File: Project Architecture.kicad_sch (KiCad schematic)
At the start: 0 parts

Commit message: Finished 65% of schematics
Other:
- sheet Section A - Title A renamed MCU - Unit
- sheet Section B - Title B renamed Power - Battery Management
- added sheet Logic - I2C Mux (Logic_I2C_Mux.kicad_sch)
- added sheet Misc - Mounting Holes & Fiducials (Misc - Mounting Holes.kicad_sch)
- added sheet Motor Control - Drivers (Motor_Control_Drivers.kicad_sch)
- added sheet Power - Path & Generation (Power_Path_Generation.kicad_sch)
- added sheet Power - Wireless Receiver & USB (Power_Wireless_Receiver_USB.kicad_sch)
- sheet MCU - Unit: file Section A - Title A.kicad_sch -> MCU_Unit.kicad_sch
- sheet Power - Battery Management: file Section B - TItle B.kicad_sch -> Power_Battery_Management.kicad_sch
- sheet Power - Battery Management ports: added +VBAT, +VCHARGE; removed none
- note added: "Page 6"
- note added: "Page 7"
- note added: "Page 9"

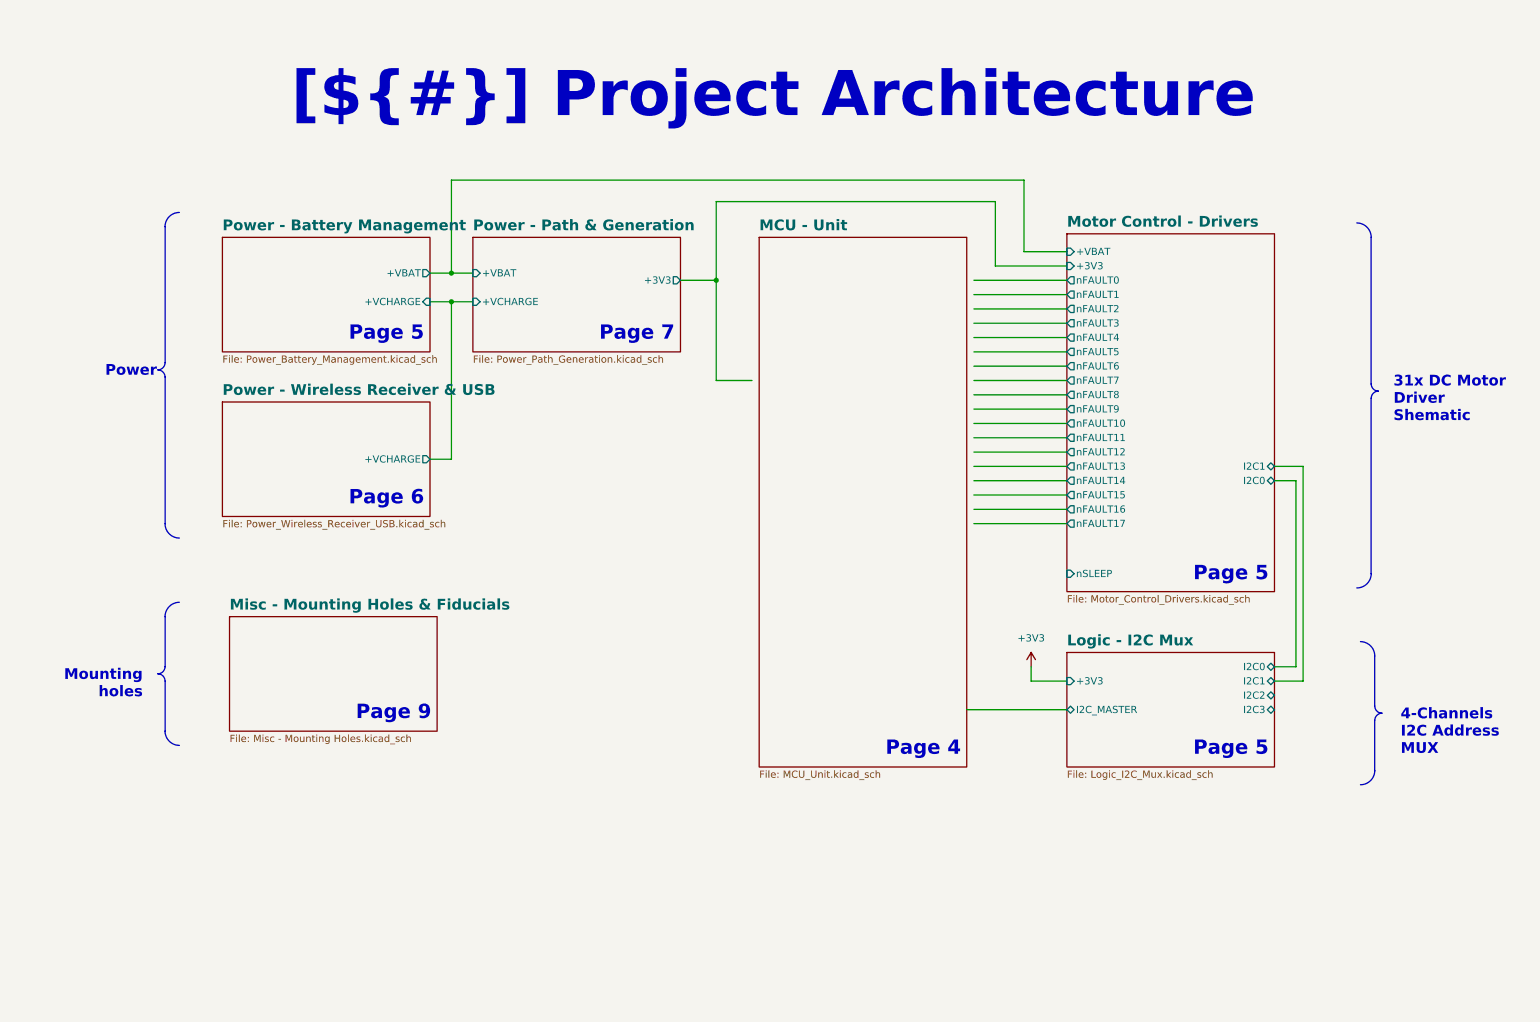
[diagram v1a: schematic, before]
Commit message: Added footprints, images, almost finished all èages except for the MCU
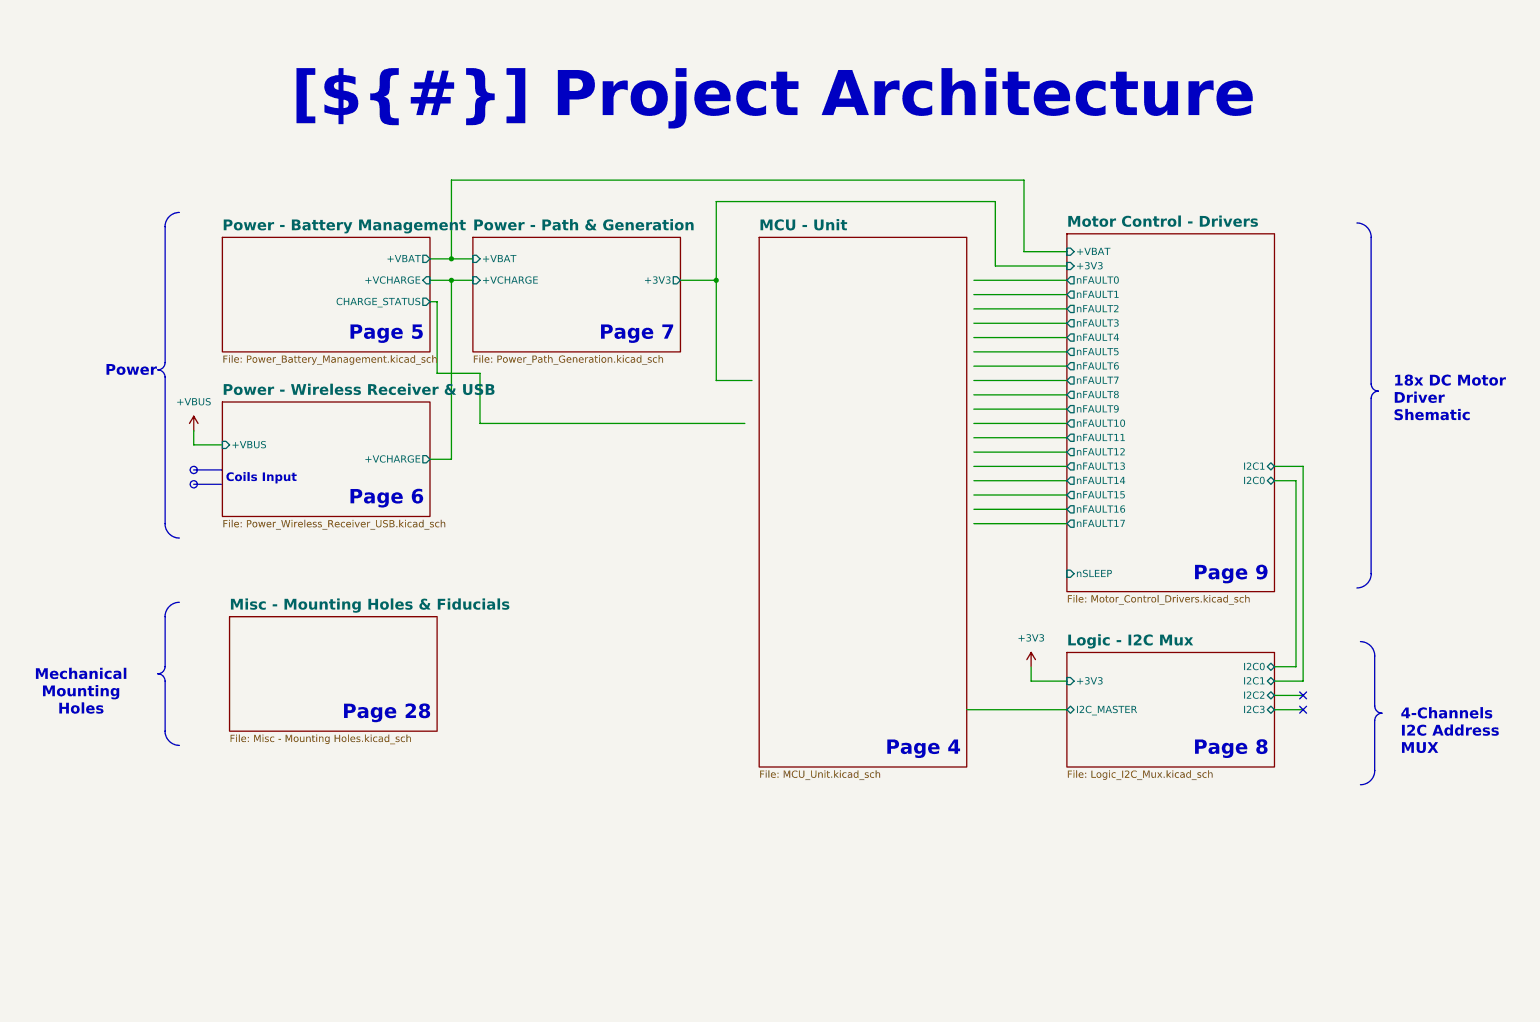
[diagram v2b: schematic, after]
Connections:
- no-connect marks 0 -> 2
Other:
- sheet Power - Battery Management ports: added CHARGE_STATUS; removed none
- sheet Power - Wireless Receiver & USB ports: added +VBUS; removed none
- note added: "Page 28"
- note added: "Page 8"

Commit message: Added RGB LED, added motor connectors, added test points, imported all 3D models
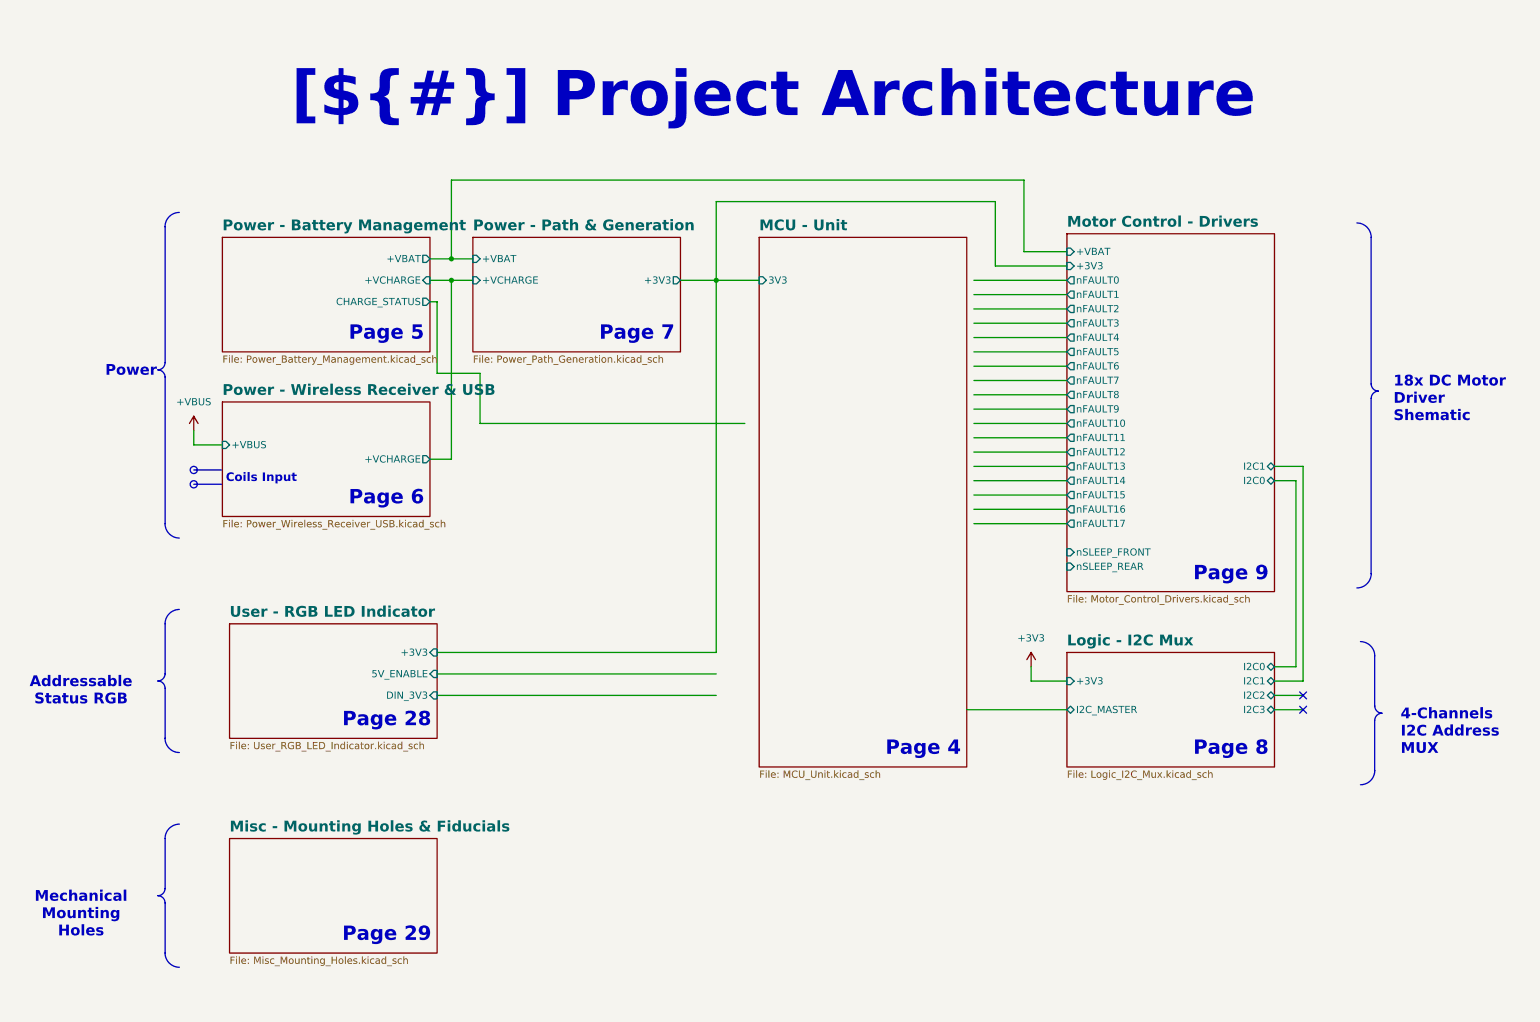
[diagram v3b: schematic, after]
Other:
- added sheet User - RGB LED Indicator (User_RGB_LED_Indicator.kicad_sch)
- sheet MCU - Unit ports: added 3V3; removed none
- sheet Misc - Mounting Holes & Fiducials: file Misc - Mounting Holes.kicad_sch -> Misc_Mounting_Holes.kicad_sch
- sheet Motor Control - Drivers ports: added nSLEEP_FRONT, nSLEEP_REAR; removed nSLEEP
- note added: "Page 29"

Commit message: Finished schematic, imported all footprints, all 3D models and created STM32 project, now need to proofread shematic before layout
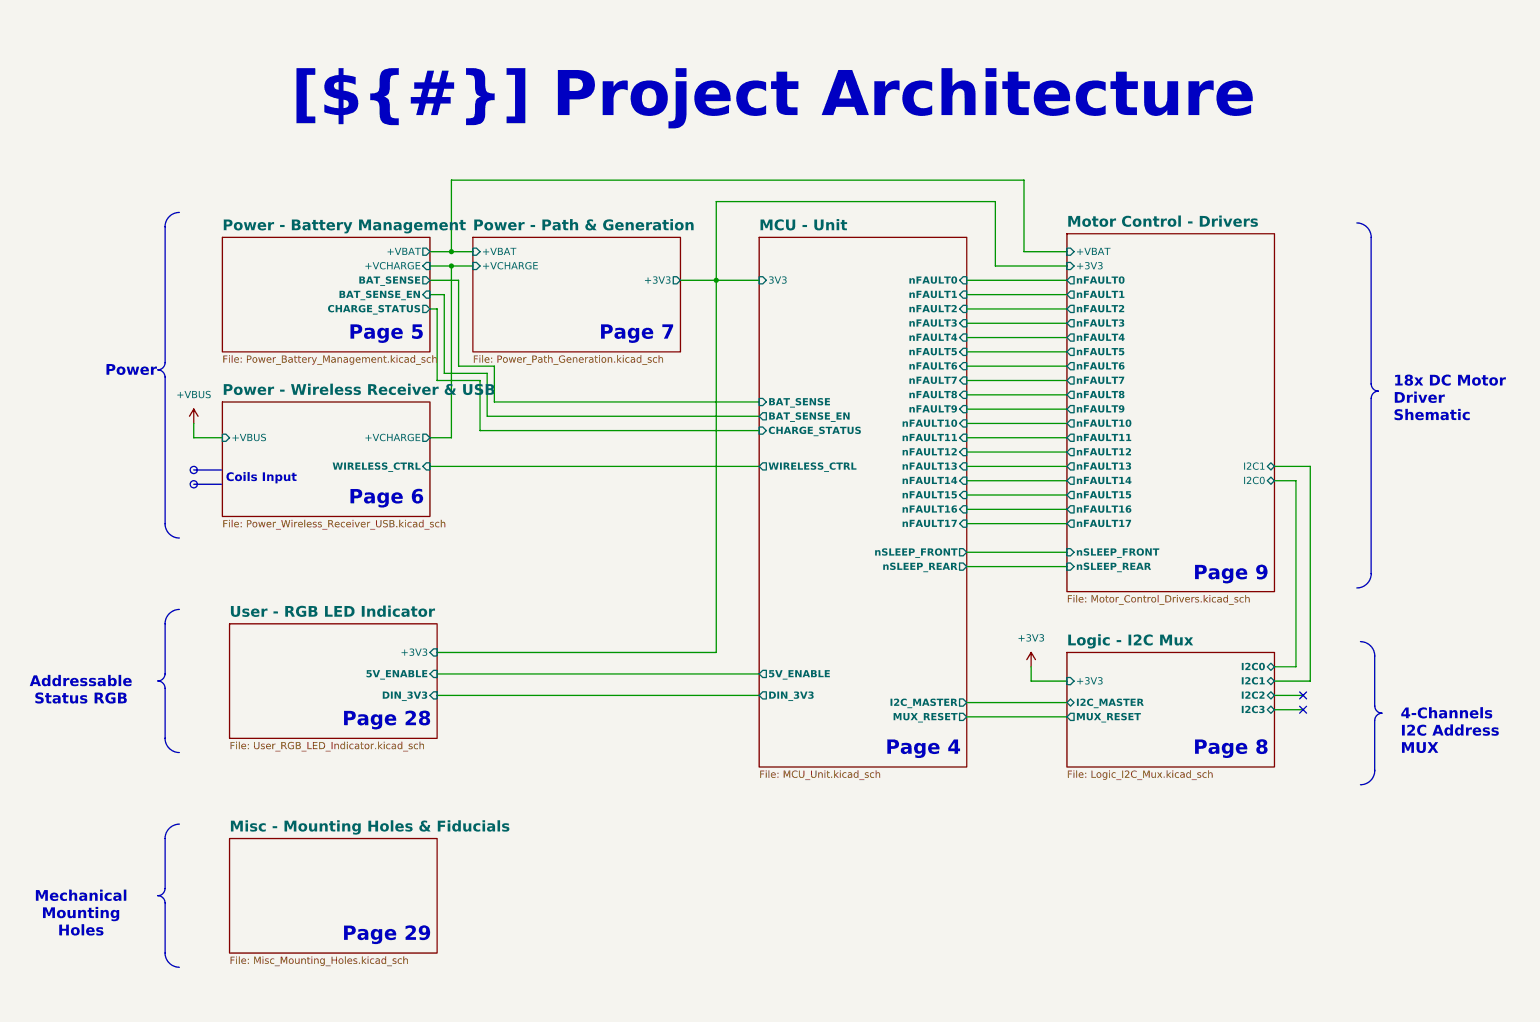
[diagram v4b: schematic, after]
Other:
- sheet Logic - I2C Mux ports: added MUX_RESET; removed none
- sheet MCU - Unit ports: added 5V_ENABLE, BAT_SENSE, BAT_SENSE_EN, CHARGE_STATUS, DIN_3V3, I2C_MASTER, MUX_RESET, WIRELESS_CTRL, nFAULT0, nFAULT1, nFAULT10, nFAULT11, nFAULT12, nFAULT13, nFAULT14, nFAULT15, nFAULT16, nFAULT17, nFAULT2, nFAULT3, nFAULT4, nFAULT5, nFAULT6, nFAULT7, nFAULT8, nFAULT9, nSLEEP_FRONT, nSLEEP_REAR; removed none
- sheet Power - Battery Management ports: added BAT_SENSE, BAT_SENSE_EN; removed none
- sheet Power - Wireless Receiver & USB ports: added WIRELESS_CTRL; removed none

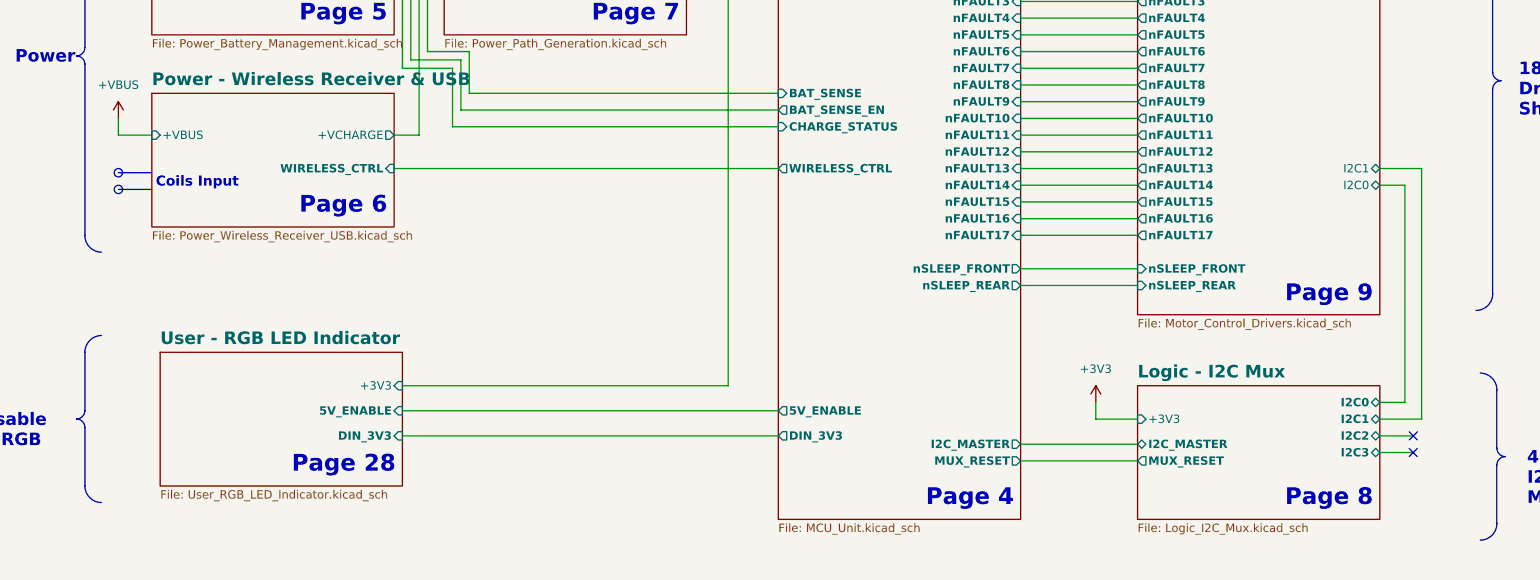
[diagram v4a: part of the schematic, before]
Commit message: Reviewed shematic, cleaned all DRC errors, chosed stackup, started layout
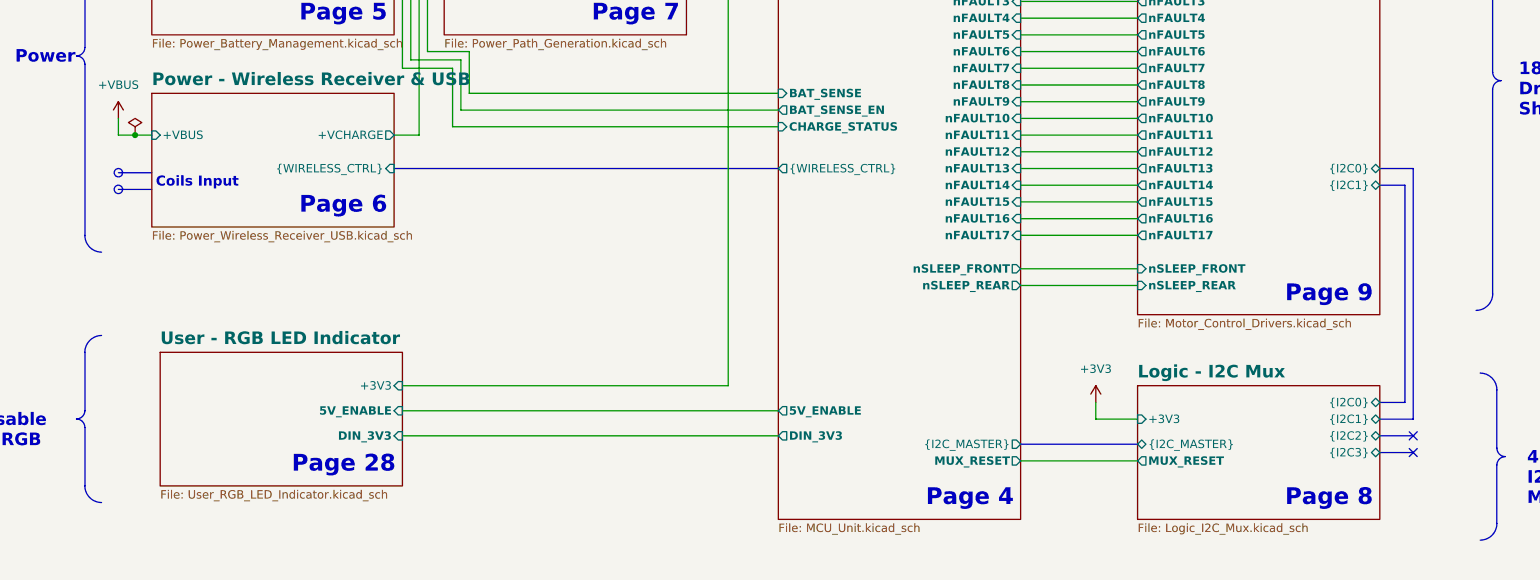
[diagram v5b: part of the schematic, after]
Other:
- sheet Logic - I2C Mux ports: added {I2C0}, {I2C1}, {I2C2}, {I2C3}, {I2C_MASTER}; removed I2C0, I2C1, I2C2, I2C3, I2C_MASTER
- sheet MCU - Unit ports: added {I2C_MASTER}, {WIRELESS_CTRL}; removed I2C_MASTER, WIRELESS_CTRL
- sheet Motor Control - Drivers ports: added {I2C0}, {I2C1}; removed I2C0, I2C1
- sheet Power - Wireless Receiver & USB ports: added {WIRELESS_CTRL}; removed WIRELESS_CTRL

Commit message: Advanced rough layout
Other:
- added sheet Sensing - IMU (Sensing_IMU.kicad_sch)
- sheet Logic - I2C Mux ports: added {I2C_MOTOR}; removed {I2C_MASTER}
- sheet MCU - Unit ports: added IMU_INT1, IMU_INT2, {I2C_MOTOR}, {I2C_SENSING}; removed {I2C_MASTER}

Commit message: Finished layout, only cleaning left
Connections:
- no-connect marks 2 -> 0
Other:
- sheet Logic - I2C Mux ports: added none; removed {I2C2}, {I2C3}
